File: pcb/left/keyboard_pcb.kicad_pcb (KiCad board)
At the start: 2 copper layers, 138.8 x 89.9 mm, 105 parts, among them J3 Alt. Battery, J4 Conn_01x01_Socket, K00 KEYSW, K01 KEYSW, K02 KEYSW, K03 KEYSW, K04 KEYSW, K05 KEYSW, K10 KEYSW, K11 KEYSW, K12 KEYSW, K13 KEYSW, K14 KEYSW, K15 KEYSW, K20 KEYSW, K21 KEYSW, K22 KEYSW, K23 KEYSW, K24 KEYSW, K25 KEYSW, K33 KEYSW, K34 KEYSW, K35 KEYSW, U1 Flippable RP2040 ProMicro/nic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

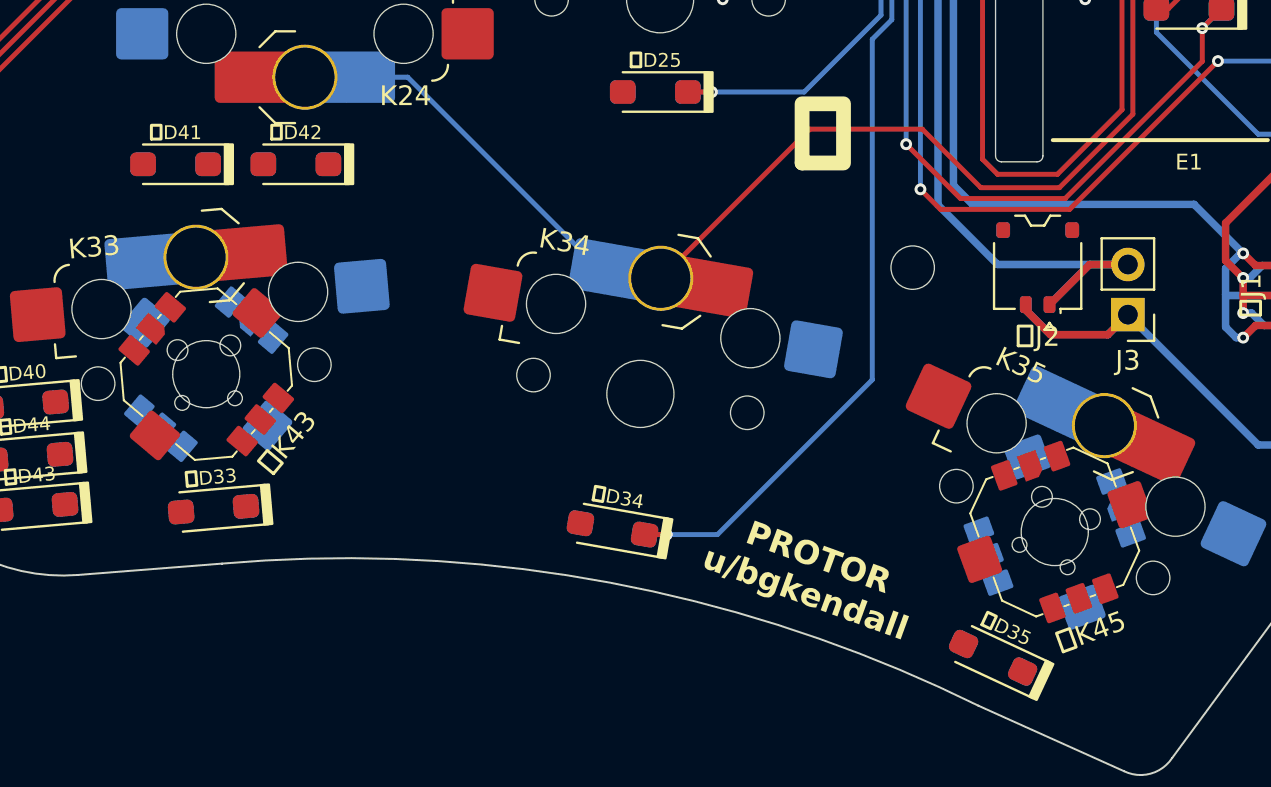
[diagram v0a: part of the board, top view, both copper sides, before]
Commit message: Tweak orientation of nav. switches and put them on the correct side
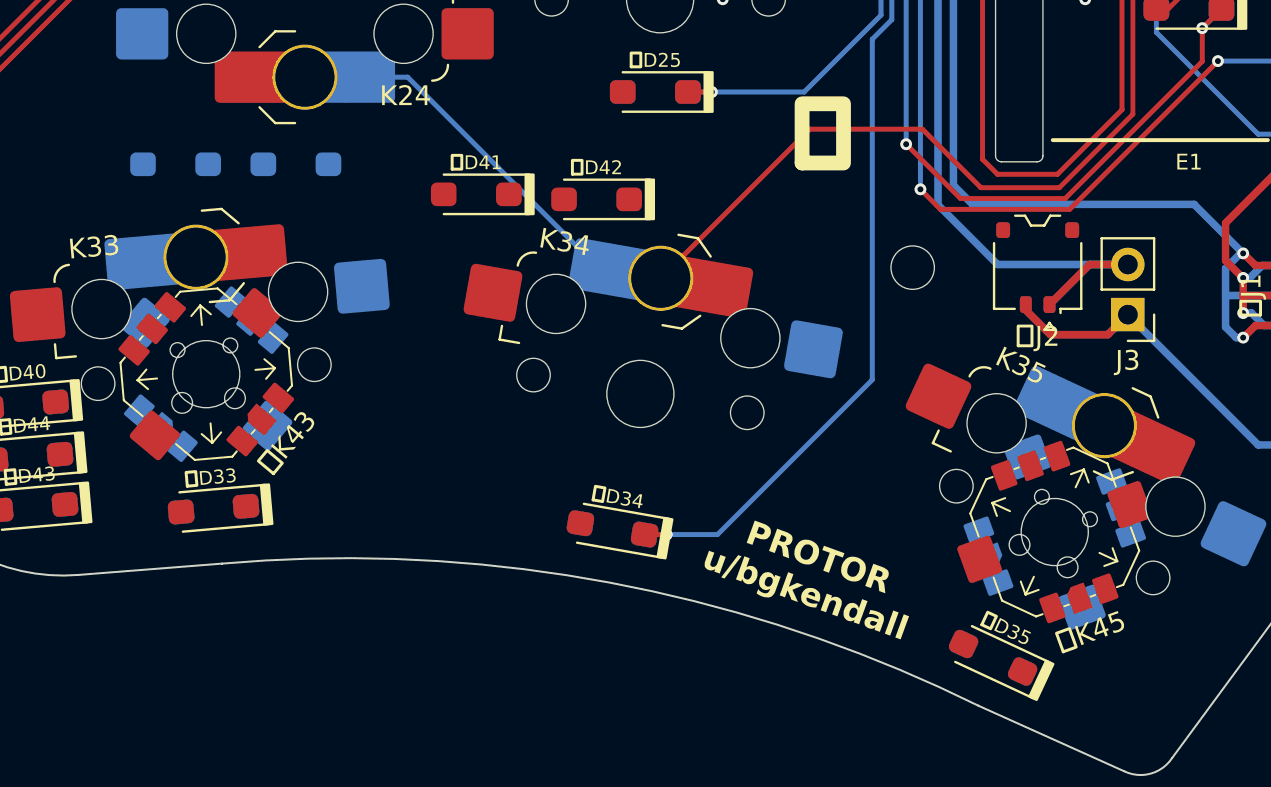
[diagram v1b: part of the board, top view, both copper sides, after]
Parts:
- 右K43, 右K45: moved to B.Cu
- 左K43, 左K45: moved to F.Cu
- moved 右D42 15.3 mm to (160.8, 104.1)
- moved 右D41 15.3 mm to (154.7, 103.9)
- turned 右K43 to -175 degrees
- turned 右K45 to 155 degrees
- turned 左K43 to 5 degrees
- turned 左K45 to -25 degrees

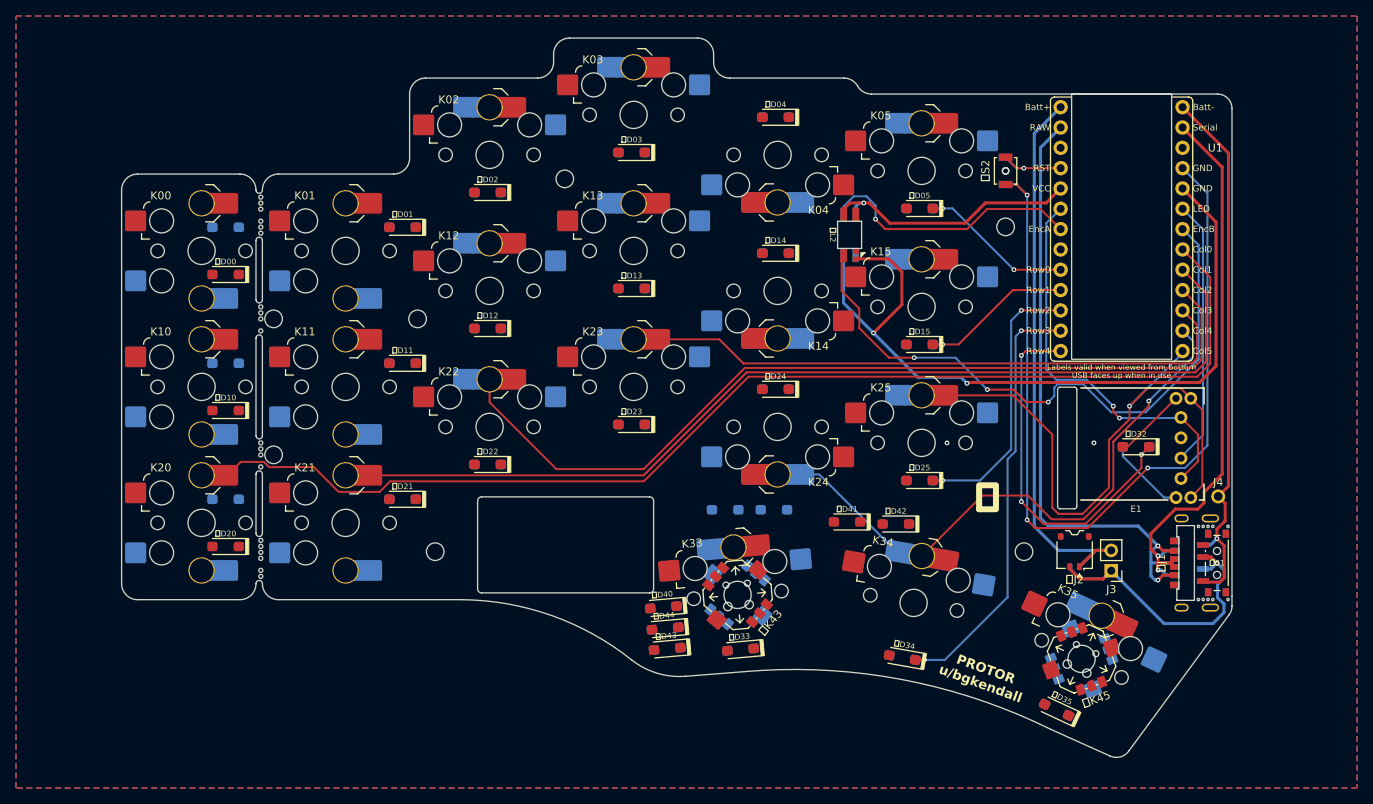
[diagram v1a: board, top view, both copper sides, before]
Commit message: Initial routing of nav. switches
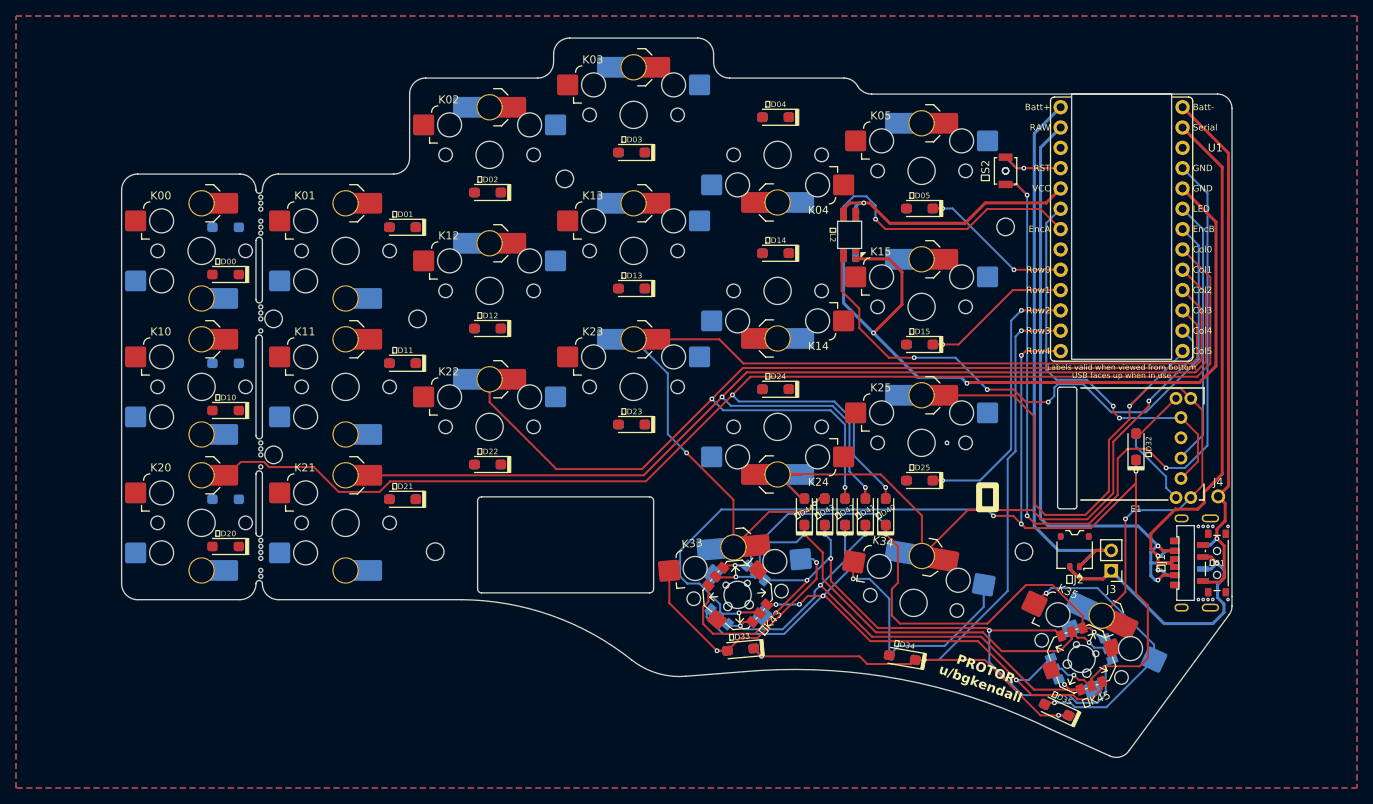
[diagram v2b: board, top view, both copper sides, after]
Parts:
- moved 右D40 30.2 mm to (159.5, 102.6), turned to 90 degrees
- moved 左D40 30.2 mm to (159.5, 102.6), turned to 90 degrees
- moved 右D43 26.1 mm to (151.9, 102.6), turned to 90 degrees
- moved 左D43 26.1 mm to (151.9, 102.6), turned to 90 degrees
- moved 右D44 22.7 mm to (149.4, 102.6), turned to 90 degrees
- moved 左D44 22.7 mm to (149.4, 102.6), turned to 90 degrees
- moved 左D41 17.5 mm to (157.0, 102.6), turned to 90 degrees
- moved 左D42 8.89 mm to (154.4, 102.6), turned to 90 degrees
- moved 右D42 6.53 mm to (154.4, 102.6), turned to 90 degrees
- moved 右D41 2.62 mm to (157.0, 102.6), turned to 90 degrees
- turned 右D32 to 90 degrees
- turned 左D32 to 90 degrees
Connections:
- 左D40 pad 1: Net-(左D40-K) -> Net-(右D40-K)
- 左D41 pad 1: Net-(左D41-K) -> Net-(右D41-K)
- 左D42 pad 1: Net-(左D42-K) -> Net-(右D42-K)
- 左D43 pad 1: Net-(左D43-K) -> Net-(右D43-K)
- 左D44 pad 1: Net-(左D44-K) -> Net-(右D44-K)
- 左K43 pad 1: Net-(左D40-K) -> Net-(右D40-K)
- 左K43 pad 2: Net-(左D44-K) -> Net-(右D44-K)
- 左K43 pad 3: Net-(左D43-K) -> Net-(右D43-K)
- 左K43 pad 4: Net-(左D41-K) -> Net-(右D41-K)
- 左K43 pad 6: Net-(左D42-K) -> Net-(右D42-K)
- 左K45 pad 1: Net-(左D40-K) -> Net-(右D40-K)
- 左K45 pad 2: Net-(左D44-K) -> Net-(右D44-K)
- 左K45 pad 3: Net-(左D43-K) -> Net-(右D43-K)
- 左K45 pad 4: Net-(左D41-K) -> Net-(右D41-K)
- 左K45 pad 6: Net-(左D42-K) -> Net-(右D42-K)
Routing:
- net row4: track 46.9 -> 147.9 mm, vias 3 -> 6
- net Net-(右D43-K): track 0.00 -> 96.8 mm, vias 0 -> 4
- net Net-(右D41-K): track 0.00 -> 85.5 mm, vias 0 -> 5
- net Net-(右D40-K): track 0.00 -> 71.1 mm, vias 0 -> 3
- net Net-(右D42-K): track 0.00 -> 67.4 mm, vias 0 -> 4
- net Net-(右D44-K): track 0.00 -> 65.6 mm, vias 0 -> 3
- net col3: track 75.4 -> 122.1 mm, vias 0 -> 2
- net row3: track 54.8 -> 100.3 mm, vias 2 -> 4
- net Net-(右D35-A): track 0.00 -> 38.3 mm, vias 0 -> 2
- net Net-(右D33-A): track 0.00 -> 34.1 mm, vias 0 -> 2
- net Net-(右D34-A): track 0.00 -> 31.8 mm, vias 0 -> 1
- net col1: track 122.9 -> 151.8 mm, vias 0 -> 2
- net col2: track 110.7 -> 139.3 mm, vias 0 -> 2
- net col0: track 149.5 -> 177.4 mm, vias 0 -> 2
- net col5: track 79.8 -> 103.9 mm, vias 1 -> 2
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
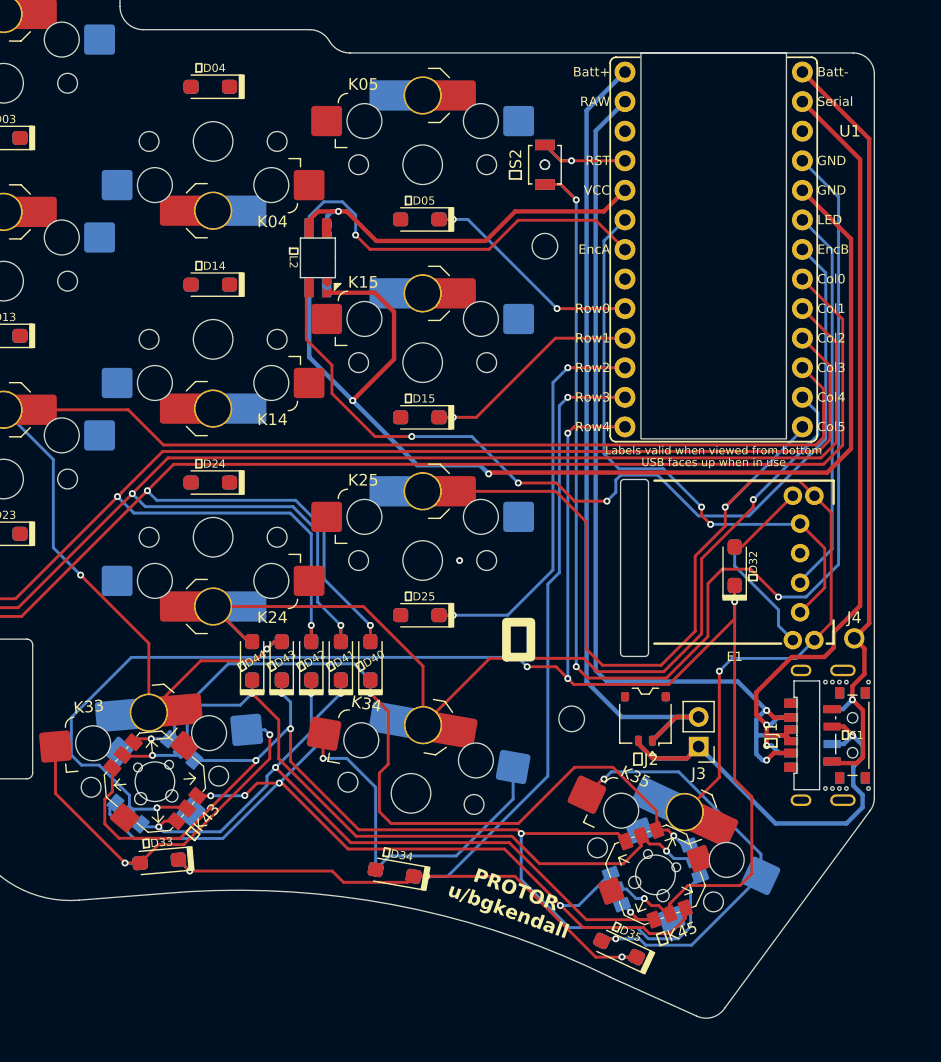
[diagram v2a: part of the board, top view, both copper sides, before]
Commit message: Move encoder diode outside encoder footprint
Want to add a standoff under the encoder, so can’t have a component there!
Updated schematic between encoder and diode to simplify routing.
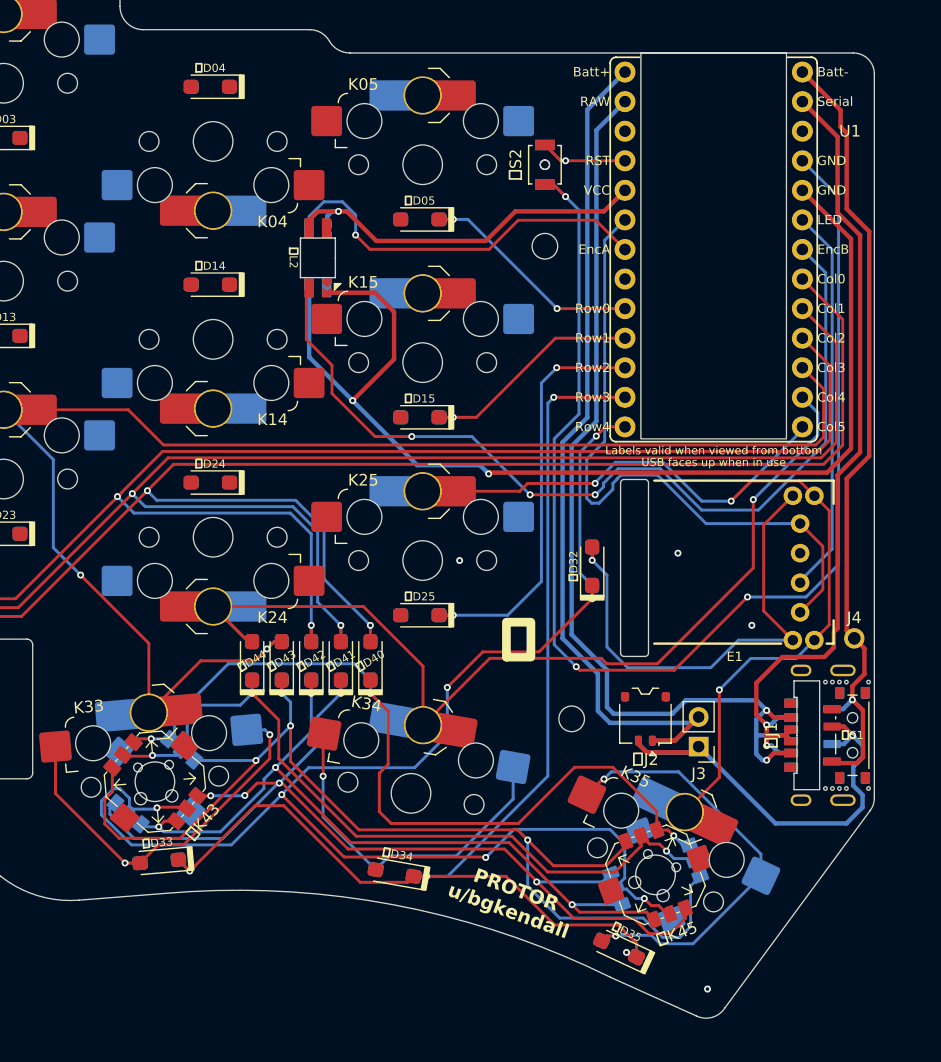
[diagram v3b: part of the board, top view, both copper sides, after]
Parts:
- moved 右D32 12.2 mm to (178.6, 94.5)
- moved 左D32 12.2 mm to (178.6, 94.5)
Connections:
- E1 pad S2: Net-(左D32-A) -> Net-(右D32-A)
- 左D32 pad 2: Net-(左D32-A) -> Net-(右D32-A)
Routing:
- net Net-(右D32-A): track 6.82 -> 42.4 mm, vias 0 -> 1
- net col5: track 103.9 -> 78.7 mm, vias 2 -> 3
- net row4: track 147.9 -> 127.2 mm, vias 6 -> 7
- net Net-(左D32-A): track 10.1 -> 0.00 mm
- net enc_a: track 49.9 -> 55.9 mm, vias 2 -> 0
- net row3: track 100.3 -> 106.1 mm
- net reset_gnd: track 114.2 -> 109.3 mm
- net l_data/r_raw: track 79.9 -> 83.9 mm
- net battery_l-/r+: track 74.2 -> 77.3 mm
- net col4: track 93.3 -> 92.0 mm
- net Net-(右D41-K): track 85.5 -> 86.6 mm
- net Net-(右D34-A): track 31.8 -> 30.7 mm
- net Net-(右D43-K): track 96.8 -> 97.9 mm
- net Net-(右D42-K): track 67.4 -> 68.4 mm
- net Net-(J3-Pin_1): track 41.3 -> 40.4 mm
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
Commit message: Connected columns
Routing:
- net col1: track 151.8 -> 202.9 mm
- net col0: track 177.4 -> 228.4 mm
- net col5: track 78.7 -> 116.4 mm, vias 3 -> 4
- net col4: track 92.0 -> 127.5 mm, vias 1 -> 2
- net col2: track 139.3 -> 173.8 mm
- net col3: track 122.1 -> 155.2 mm, vias 2 -> 1
- net r_led: track 78.5 -> 79.5 mm

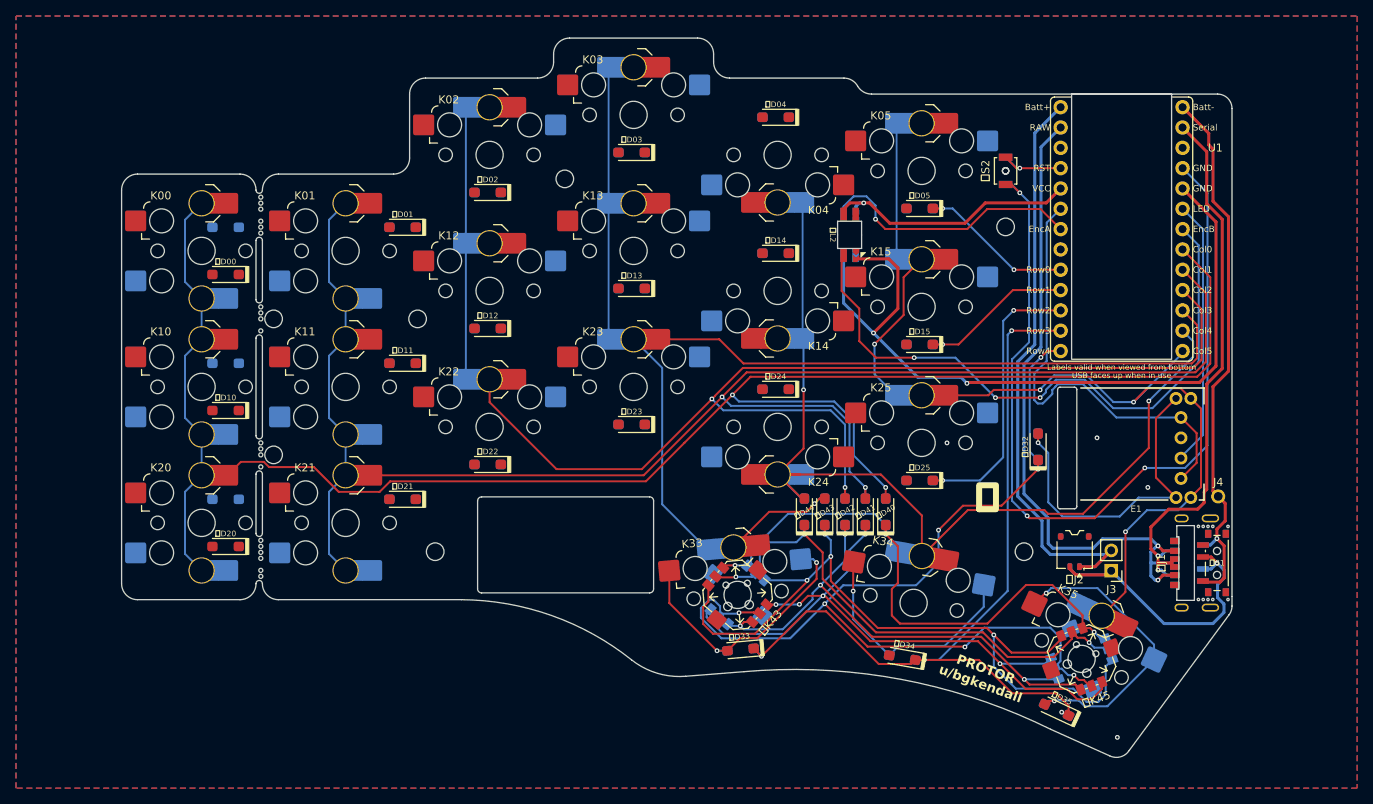
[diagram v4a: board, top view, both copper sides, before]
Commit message: Connect rows
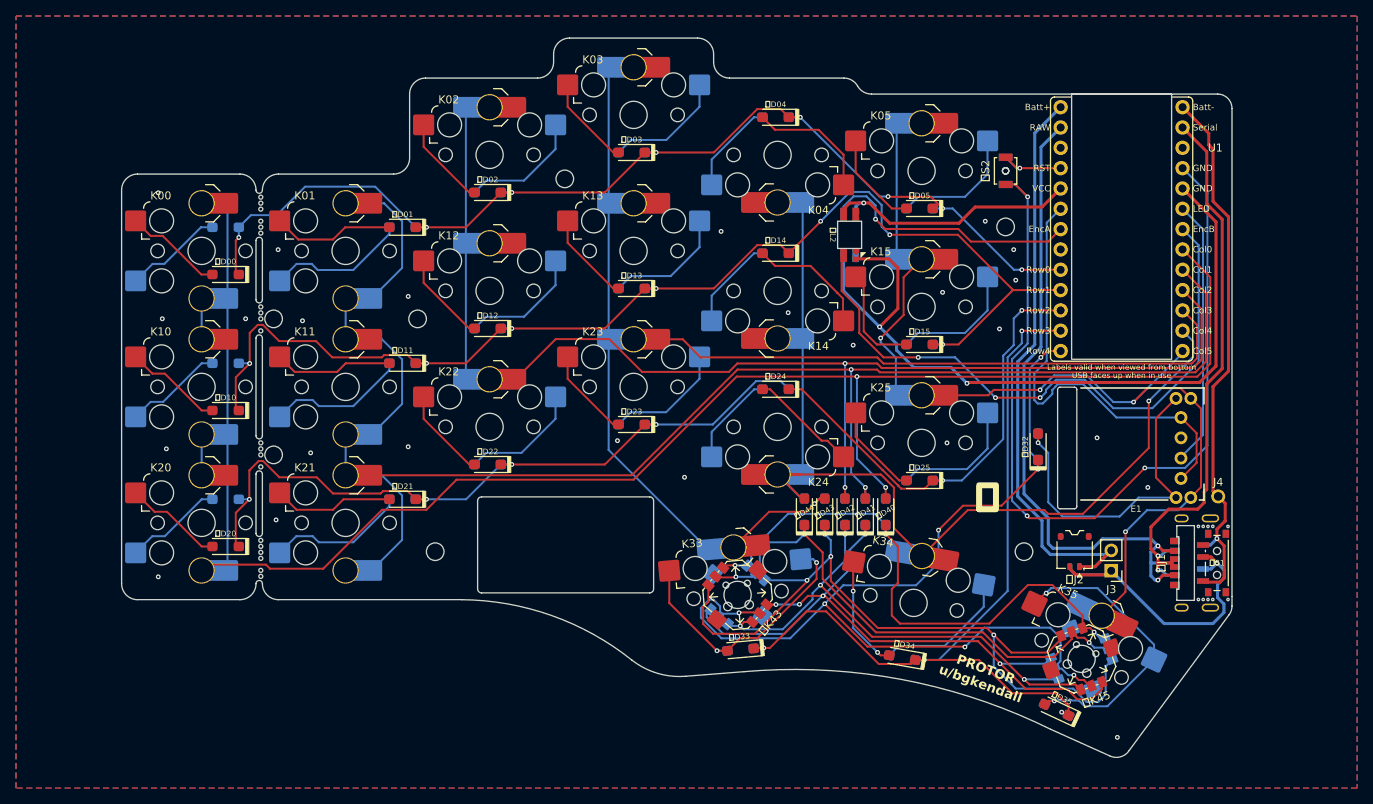
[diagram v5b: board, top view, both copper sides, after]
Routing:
- net row1: track 20.0 -> 150.5 mm, vias 1 -> 7
- net row2: track 36.0 -> 150.1 mm, vias 2 -> 6
- net row0: track 20.4 -> 134.4 mm, vias 2 -> 8
- net Net-(右D01-A): track 0.00 -> 32.9 mm
- net Net-(右D21-A): track 0.00 -> 32.8 mm
- net Net-(右D11-A): track 0.00 -> 32.6 mm
- net Net-(右D15-A): track 0.00 -> 29.3 mm
- net Net-(右D05-A): track 0.00 -> 28.2 mm
- net Net-(右D25-A): track 0.00 -> 27.9 mm
- net Net-(右D04-A): track 0.00 -> 27.6 mm
- net Net-(右D13-A): track 0.00 -> 27.0 mm
- net Net-(右D14-A): track 0.00 -> 26.9 mm
- net Net-(右D12-A): track 0.00 -> 26.9 mm
- net Net-(右D02-A): track 0.00 -> 26.9 mm
- net Net-(右D23-A): track 0.00 -> 26.7 mm
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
